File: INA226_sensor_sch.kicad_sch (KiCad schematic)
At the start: 6 parts, among them U10 INA226AIDGSR, U11 INA226AIDGSR

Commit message: C14 y C1,C2,... modificados
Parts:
- C39, C40: LCSC Part C5448844 -> C282518
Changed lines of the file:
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@@
+			)
+		)
+		(property "Field7" ""
+			(at 58.42 78.74 90)
+			(hide yes)
+			(show_name no)
+			(do_not_autoplace no)
+			(effects
+				(font
+					(size 1.27 1.27)
+				)
 			)
 		)
@@
 			)
 		)
+		(property "Field7" ""
+			(at 184.15 74.93 0)
+			(hide yes)
+			(show_name no)
+			(do_not_autoplace no)
+			(effects
+				(font
+					(size 1.27 1.27)
+				)
+			)
+		)
 		(pin "1"
 		)
@@
 			)
 		)
+		(property "Field7" ""
+			(at 220.98 78.74 90)
+			(hide yes)
+			(show_name no)
+			(do_not_autoplace no)
+			(effects
+				(font
+					(size 1.27 1.27)
+				)
+			)
+		)
 		(pin "2"
 		)
@@
 		(property "LCSC Part" "C49851"
 			(at 118.11 97.79 0)
+			(hide yes)
+			(show_name no)
+			(do_not_autoplace no)
+			(effects
+				(font
+					(size 1.27 1.27)
+				)
+			)
+		)
+		(property "Field7" ""
+			(at 118.11 74.93 0)
 			(hide yes)
 			(show_name no)
@@
 			)
 		)
-		(property "Datasheet" "https://www.lcsc.com/datasheet/C5448844.pdf"
+		(property "Datasheet" "https://www.lcsc.com/datasheet/C282518.pdf?spm=wm.sxq.inf.ggs___wm.fly.bg.0.cbh&lcsc_vid=FVBZXlJVElFWAVdTTgAPVAcHR1hXAlIFT1cMUAFWQVYxVlNeRFBfVlJeQ1VXXzsOAxUeFF5JWBYZEEoKFBINSQcJGk4NBhADEA4cHktXRlVcSQwSGg0%3D"
 			(at 95.25 93.98 0)
 			(hide yes)
@@
 			)
 		)
-		(property "LCSC Part" "C5448844"
+		(property "LCSC Part" "C282518"
 			(at 102.87 93.98 0)
+			(hide yes)
+			(show_name no)
+			(do_not_autoplace no)
+			(effects
+				(font
+					(size 1.27 1.27)
+				)
+			)
+		)
+		(property "Field7" ""
+			(at 85.09 93.98 90)
 			(hide yes)
 			(show_name no)
@@
 			)
 		)
-		(property "Datasheet" "https://www.lcsc.com/datasheet/C5448844.pdf"
+		(property "Datasheet" "https://www.lcsc.com/datasheet/C282518.pdf?spm=wm.sxq.inf.ggs___wm.fly.bg.0.cbh&lcsc_vid=FVBZXlJVElFWAVdTTgAPVAcHR1hXAlIFT1cMUAFWQVYxVlNeRFBfVlJeQ1VXXzsOAxUeFF5JWBYZEEoKFBINSQcJGk4NBhADEA4cHktXRlVcSQwSGg0%3D"
 			(at 163.83 92.71 0)
 			(hide yes)
@@
 			)
 		)
-		(property "LCSC Part" "C5448844"
+		(property "LCSC Part" "C282518"
 			(at 171.45 92.71 0)
 			(hide yes)
 			(show_name no)
+			(do_not_autoplace no)
+			(effects
+				(font
+					(size 1.27 1.27)
+				)
+			)
+		)
+		(property "Field7" ""
+			(at 153.67 92.71 90)
+			(hide yes)
+			(show_name no)

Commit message: correcciones claude
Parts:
- added R11: 30mΩ 1W, Resistor_SMD:R_1206_3216Metric_Pad1.30x1.75mm_HandSolder, symbol Device:R
- added R22: 6mΩ 2W, Resistor_SMD:R_2512_6332Metric_Pad1.40x3.35mm_HandSolder, symbol Device:R
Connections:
- net VIN2+: now also U11.10 (VIN+), R22.1
- net VINS2+: now reaches U11.9 (VIN-)
- net VINS2+: now also R22.2
- net at U10.10 (VIN+): now also R11.1
- net at U10.9 (VIN-): now also R11.2
- no-connect marks 4 -> 0

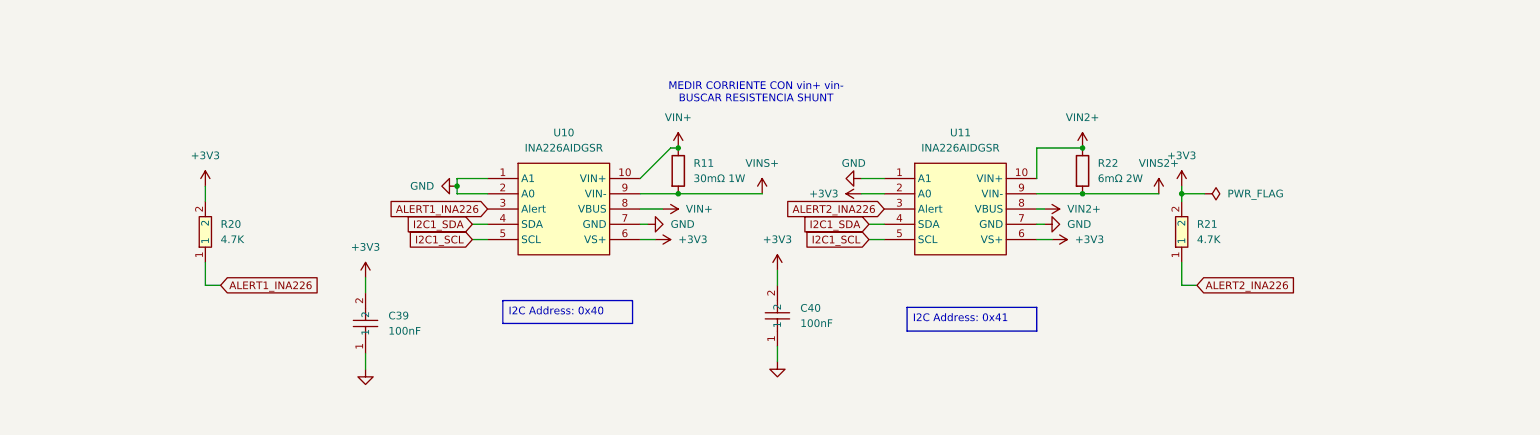
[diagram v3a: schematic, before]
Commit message: INA226 SOLUCIONADO
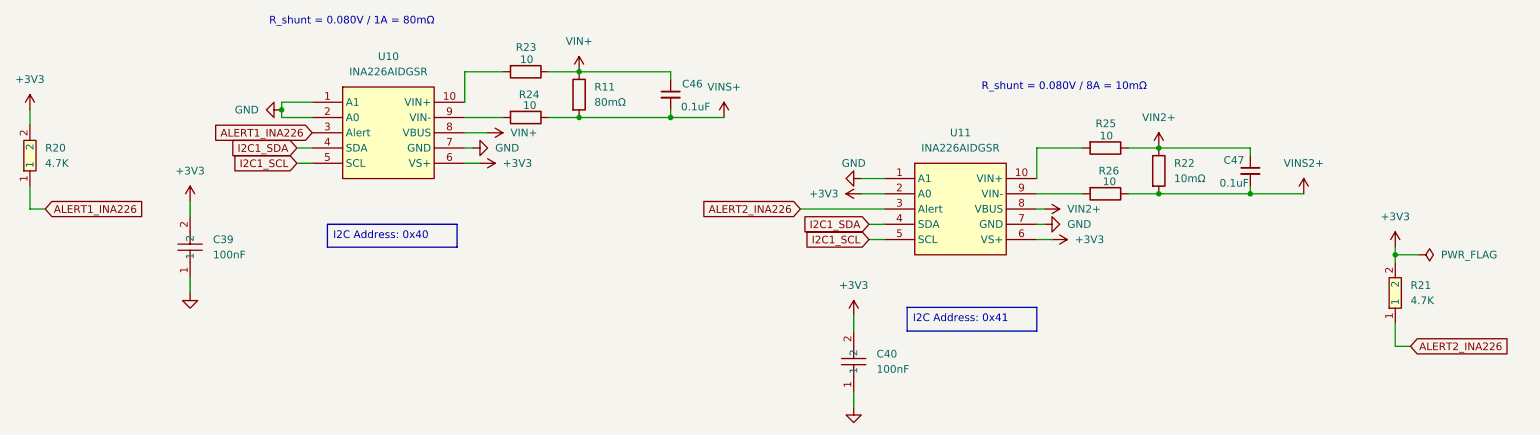
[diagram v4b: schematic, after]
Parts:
- added C46, C47: 0.1uF, Capacitor_SMD:C_0603_1608Metric_Pad1.08x0.95mm_HandSolder, symbol Device:C_Small
- added R23, R24, R25, R26: 10, Resistor_SMD:R_0603_1608Metric_Pad0.98x0.95mm_HandSolder, symbol Device:R
- R11: value 30mΩ 1W -> 80mΩ
- R22: value 6mΩ 2W -> 10mΩ
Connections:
- net VIN2+: now also C47.1, R25.1; no longer U11.10 (VIN+)
- net VINS2+: now also C47.2, R26.1; no longer U11.9 (VIN-)
- net at R11.1: now also C46.1, R23.1; no longer U10.10 (VIN+)
- net at R11.2: now also C46.2, R24.1; no longer U10.9 (VIN-)
- new net: R25.2, U11.10 (VIN+)
- new net: R26.2, U11.9 (VIN-)
- new net: R23.2, U10.10 (VIN+)
- new net: R24.2, U10.9 (VIN-)
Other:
- note added: "R_shunt = 0.080V / 1A = 80mΩ"
- note added: "R_shunt = 0.080V / 8A = 10mΩ"
- note removed: "MEDIR CORRIENTE CON vin+ vin- BUSCAR RESISTENCIA SHUNT"
- moved on the sheet: C39, C40, R11, R20, R21, U10

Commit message: 08/08
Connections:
- net VINS2+: now also U11.8 (VBUS); no longer C47.2, R22.2, R26.1
- net +VINP: now reaches C46.1, R11.1, R23.1
- net VIN2+ renamed +VIN2P
- net +VIN2P: no longer U11.8 (VBUS)
- new net +11.1V: C47.2, R22.2, R26.1
